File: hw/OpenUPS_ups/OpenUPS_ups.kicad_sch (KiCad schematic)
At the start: 5 parts, among them J101 XT60PW-M, U101 AVR32DB28x-xSO

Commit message: Work on Buck Boosts
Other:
- note added: "Analog Out"

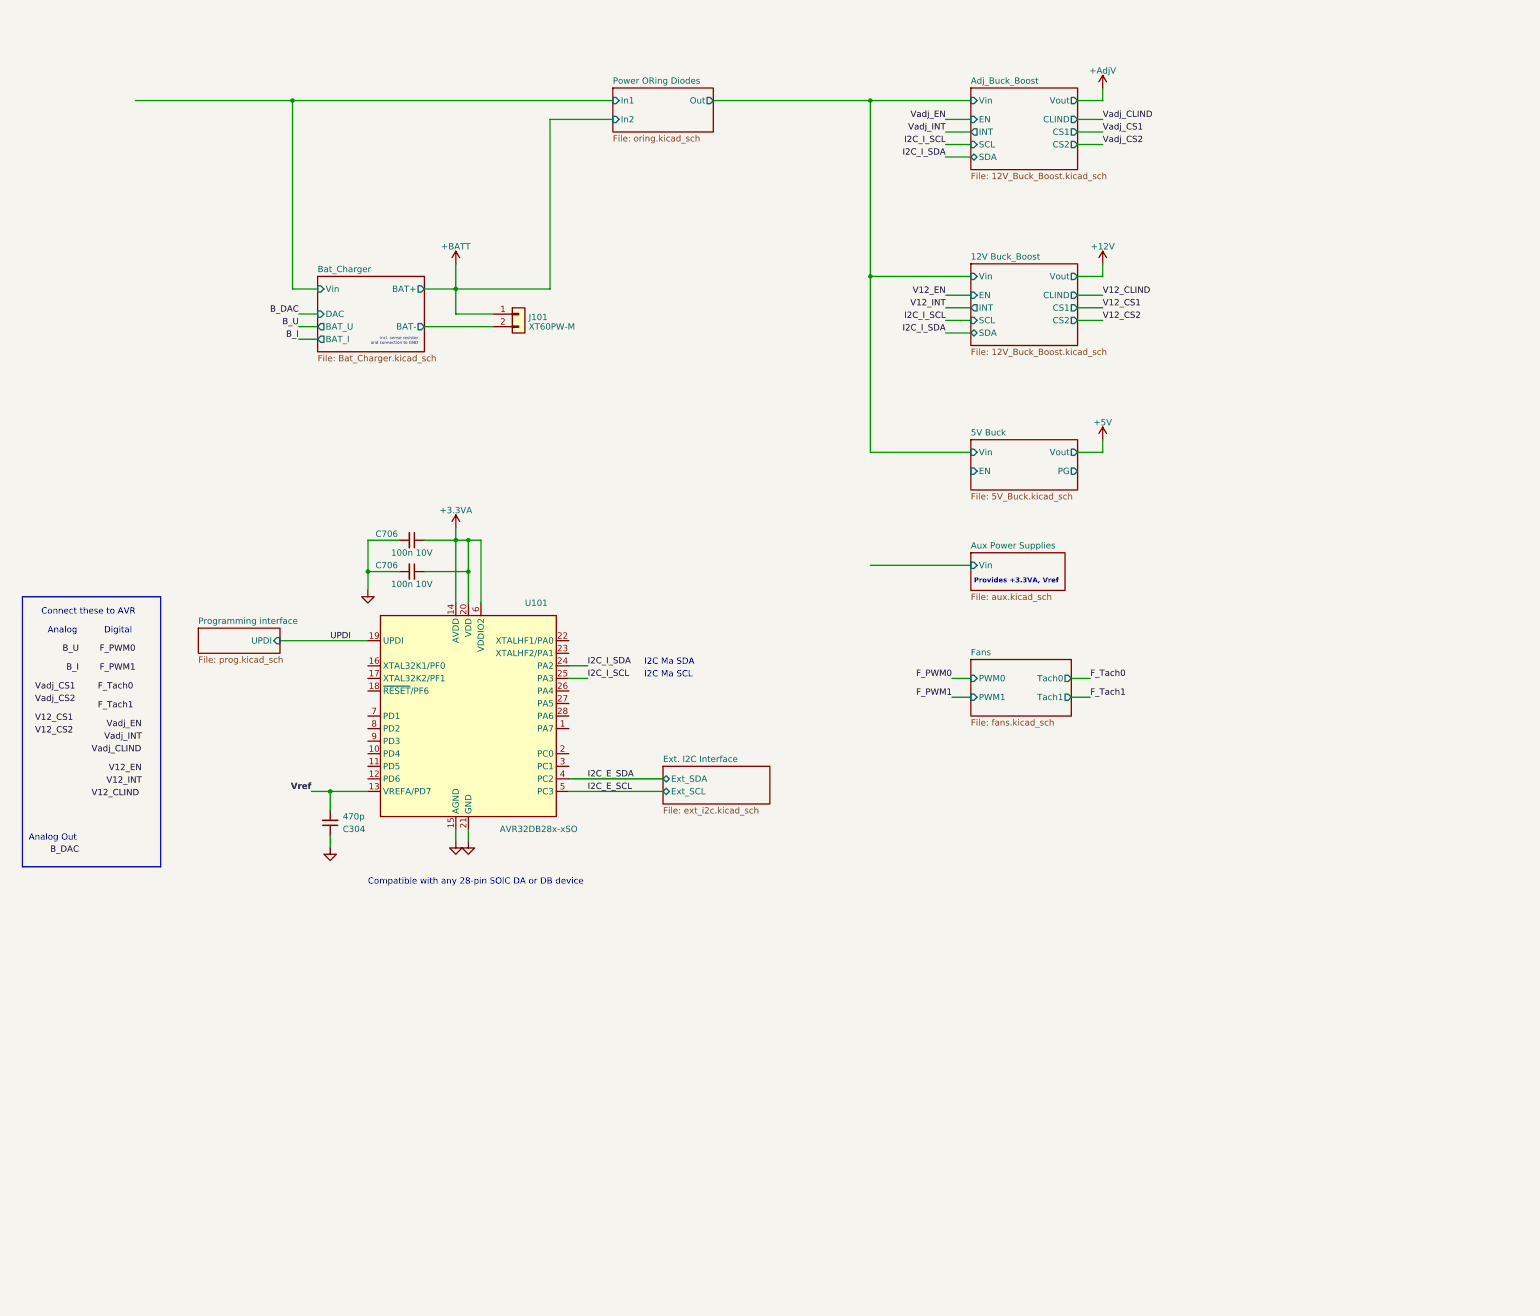
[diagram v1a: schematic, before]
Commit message: Work on 5V; EN pins taken care of.
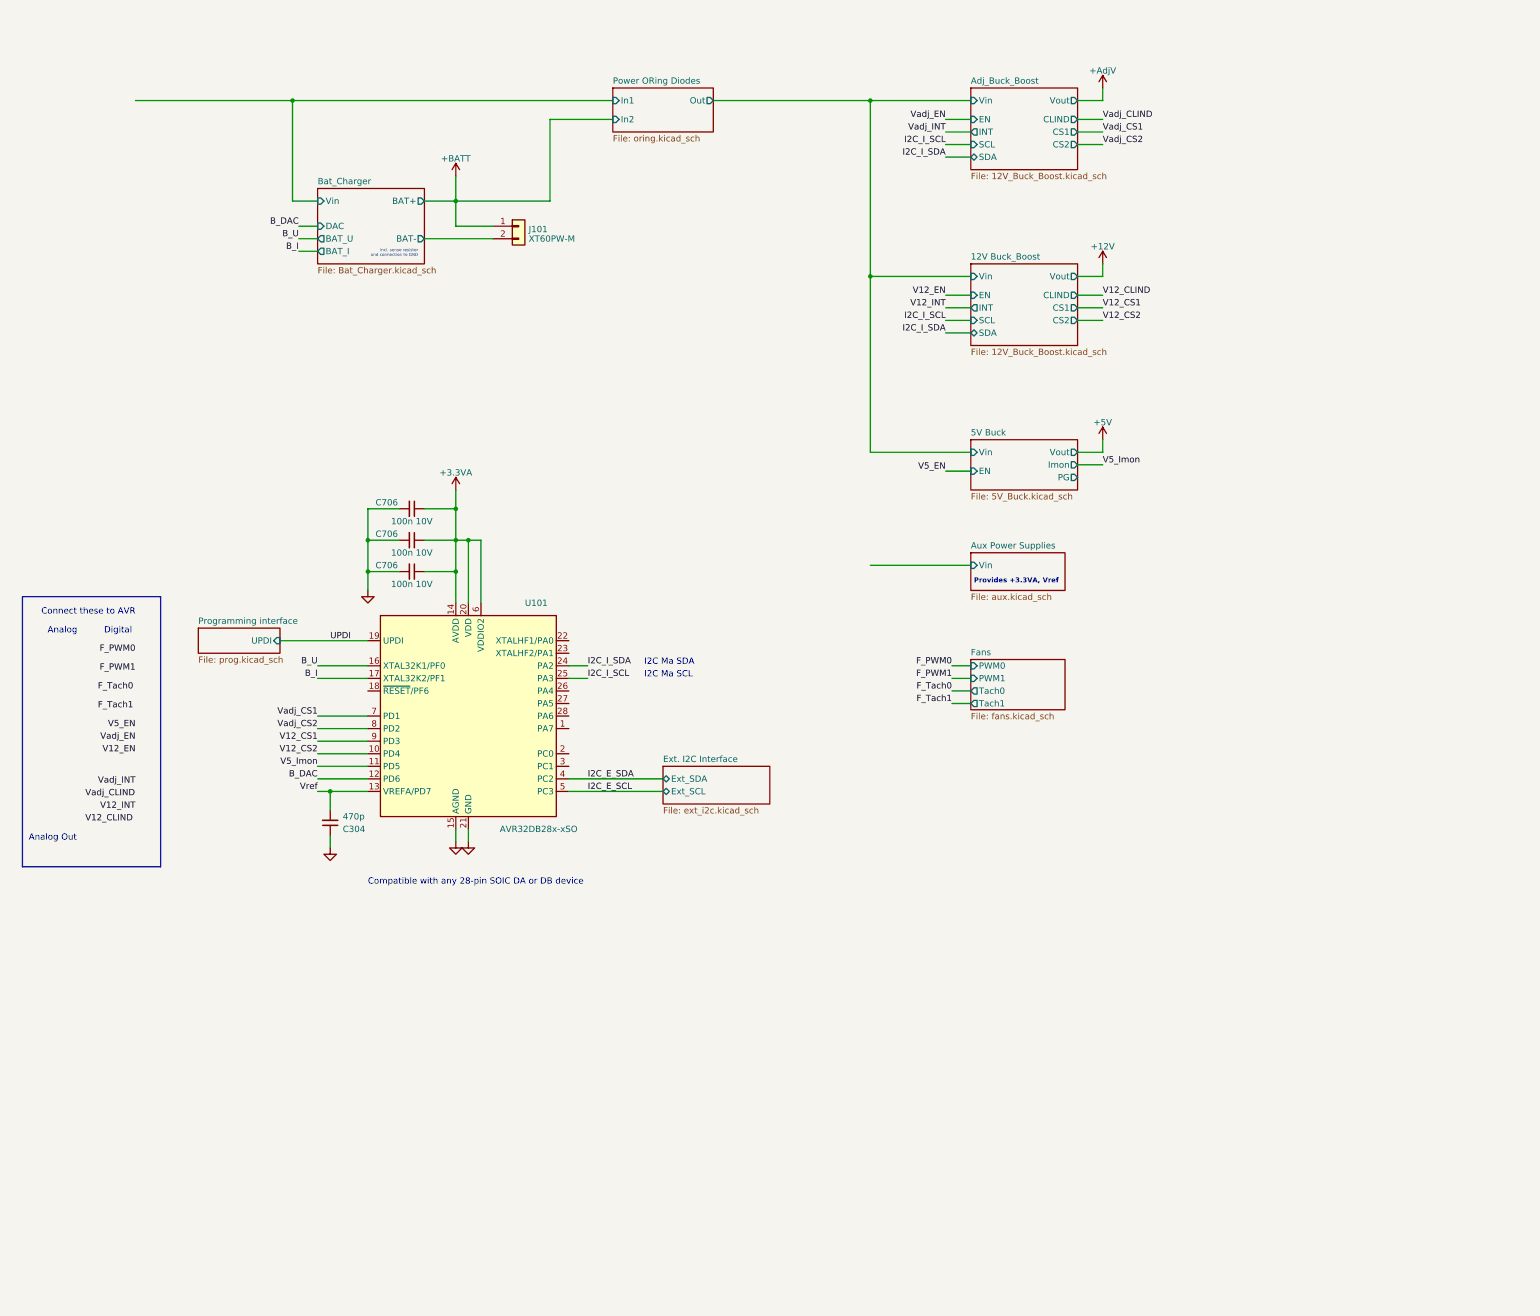
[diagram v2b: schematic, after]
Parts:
- added C706: 100n 10V, Capacitor_SMD:C_0603_1608Metric, symbol Device:C_Small
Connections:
- net +3.3VA: now also C706.1
- net B_DAC: now also U101.12 (PD6)
- net B_I: now also U101.17 (XTAL32K2/PF1)
- net B_U: now also U101.16 (XTAL32K1/PF0)
- net GND: now also C706.2
- net V12_CS1: now also U101.9 (PD3)
- net V12_CS2: now also U101.10 (PD4)
- net Vadj_CS1: now also U101.7 (PD1)
- net Vadj_CS2: now also U101.8 (PD2)
- net V5_Imon: now reaches U101.11 (PD5)
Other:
- sheet 5V Buck ports: added Imon; removed none
- moved on the sheet: J101

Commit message: Added ports and fuses
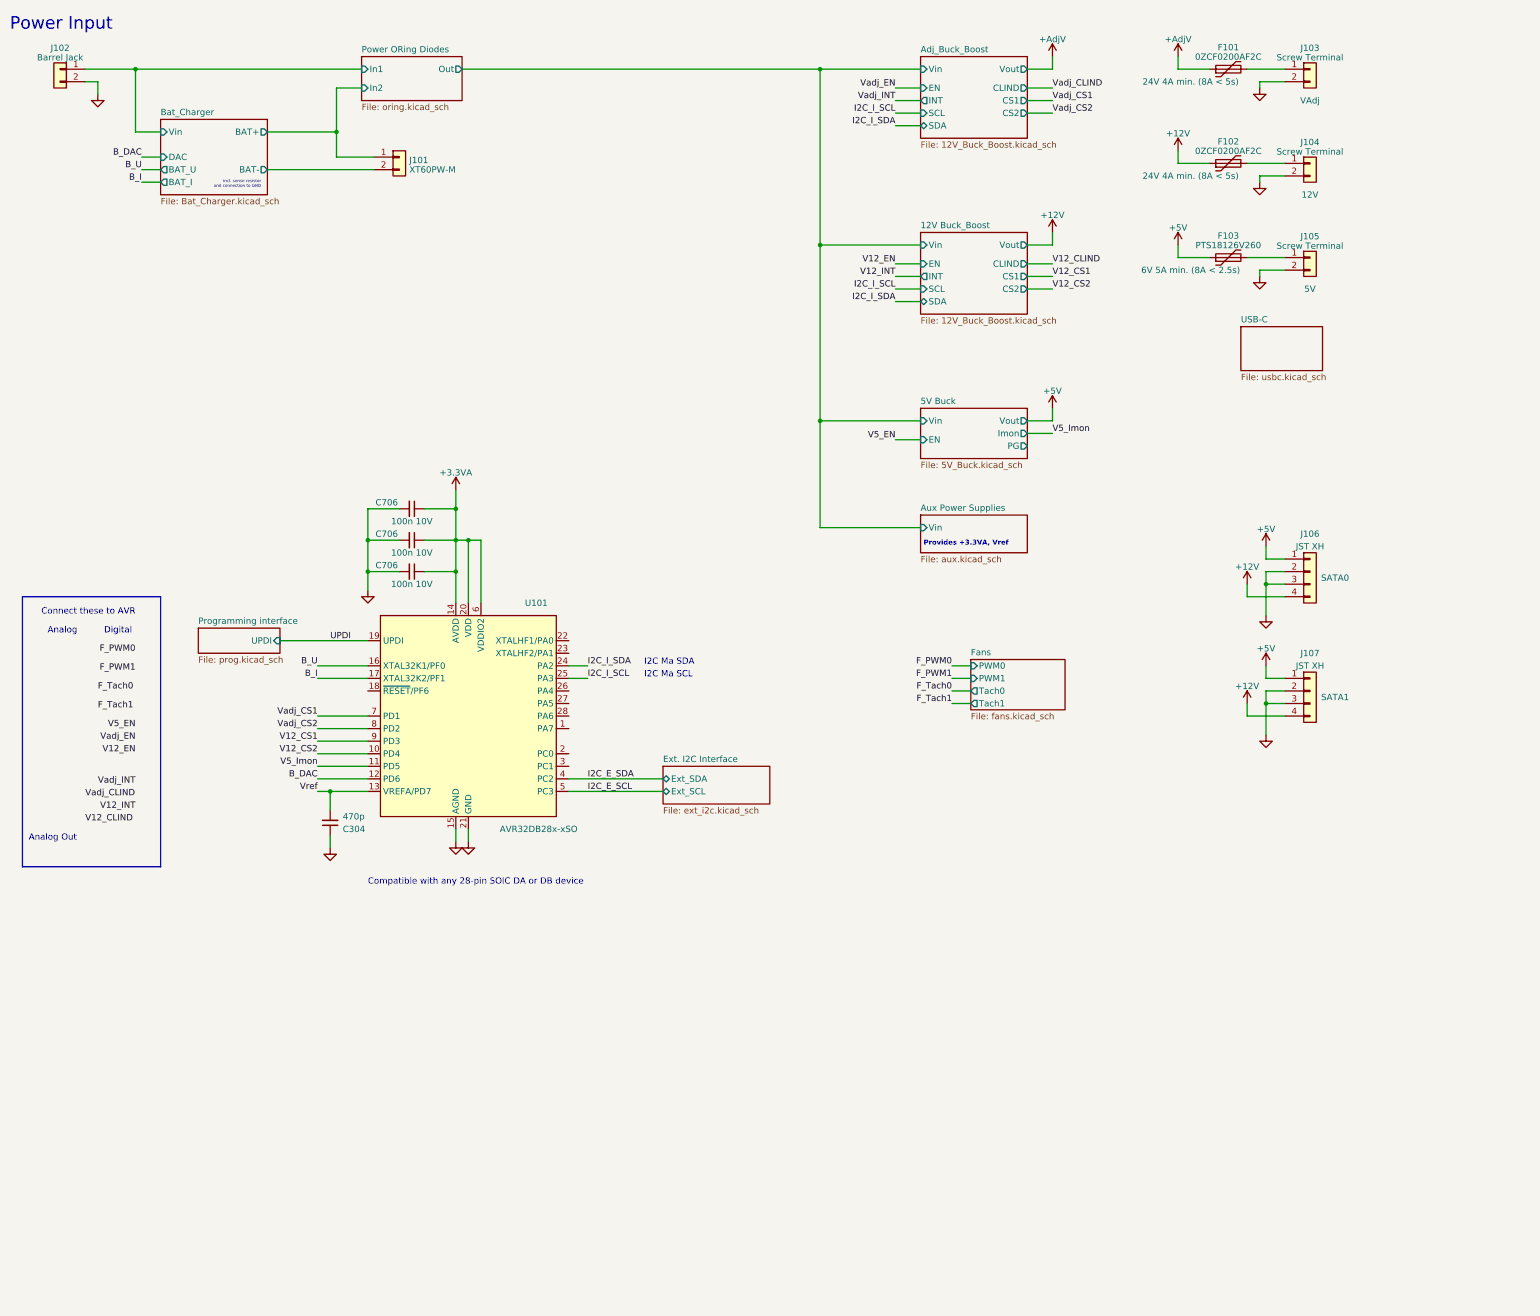
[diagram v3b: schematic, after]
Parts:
- added F101, F102: 0ZCF0200AF2C, Fuse:Fuse_2920_7451Metric, symbol Device:Polyfuse
- added F103: PTS18126V260, Fuse:Fuse_1812_4532Metric, symbol Device:Polyfuse
- added J102: Barrel Jack, Connector_BarrelJack:BarrelJack_CUI_PJ-063AH_Horizontal, symbol Connector_Generic:Conn_01x02
- added J103, J104, J105: Screw Terminal, screw_term:691213710002, symbol Connector_Generic:Conn_01x02
- added J106, J107: JST XH, Connector_JST:JST_XH_S4B-XH-A_1x04_P2.50mm_Horizontal, symbol Connector_Generic:Conn_01x04
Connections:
- net +12V: now also F102.1, J106.4 (Pin_4), J107.4 (Pin_4)
- net +5V: now also F103.1, J106.1 (Pin_1), J107.1 (Pin_1)
- net +AdjV: now also F101.1
- net Bat_Charger/Vin: now also J102.1 (Pin_1)
- net GND: now also J102.2 (Pin_2), J103.2 (Pin_2), J104.2 (Pin_2), J105.2 (Pin_2), J106.2 (Pin_2), J106.3 (Pin_3), J107.2 (Pin_2), J107.3 (Pin_3)
- net +BATT renamed Bat_Charger/BAT+
- new net: F102.2, J104.1 (Pin_1)
- new net: F101.2, J103.1 (Pin_1)
- new net: F103.2, J105.1 (Pin_1)
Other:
- added sheet USB-C (usbc.kicad_sch)
- note added: "Power Input"
- moved on the sheet: J101

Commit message: Issue #17
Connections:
- net Bat_Charger/Vin renamed Aux Power Supplies/EN2
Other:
- sheet Aux Power Supplies ports: added EN1, EN2; removed none
- moved on the sheet: C304, C706, F101, F102, F103, J101, J102, J103, J104, J105, J106, J107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

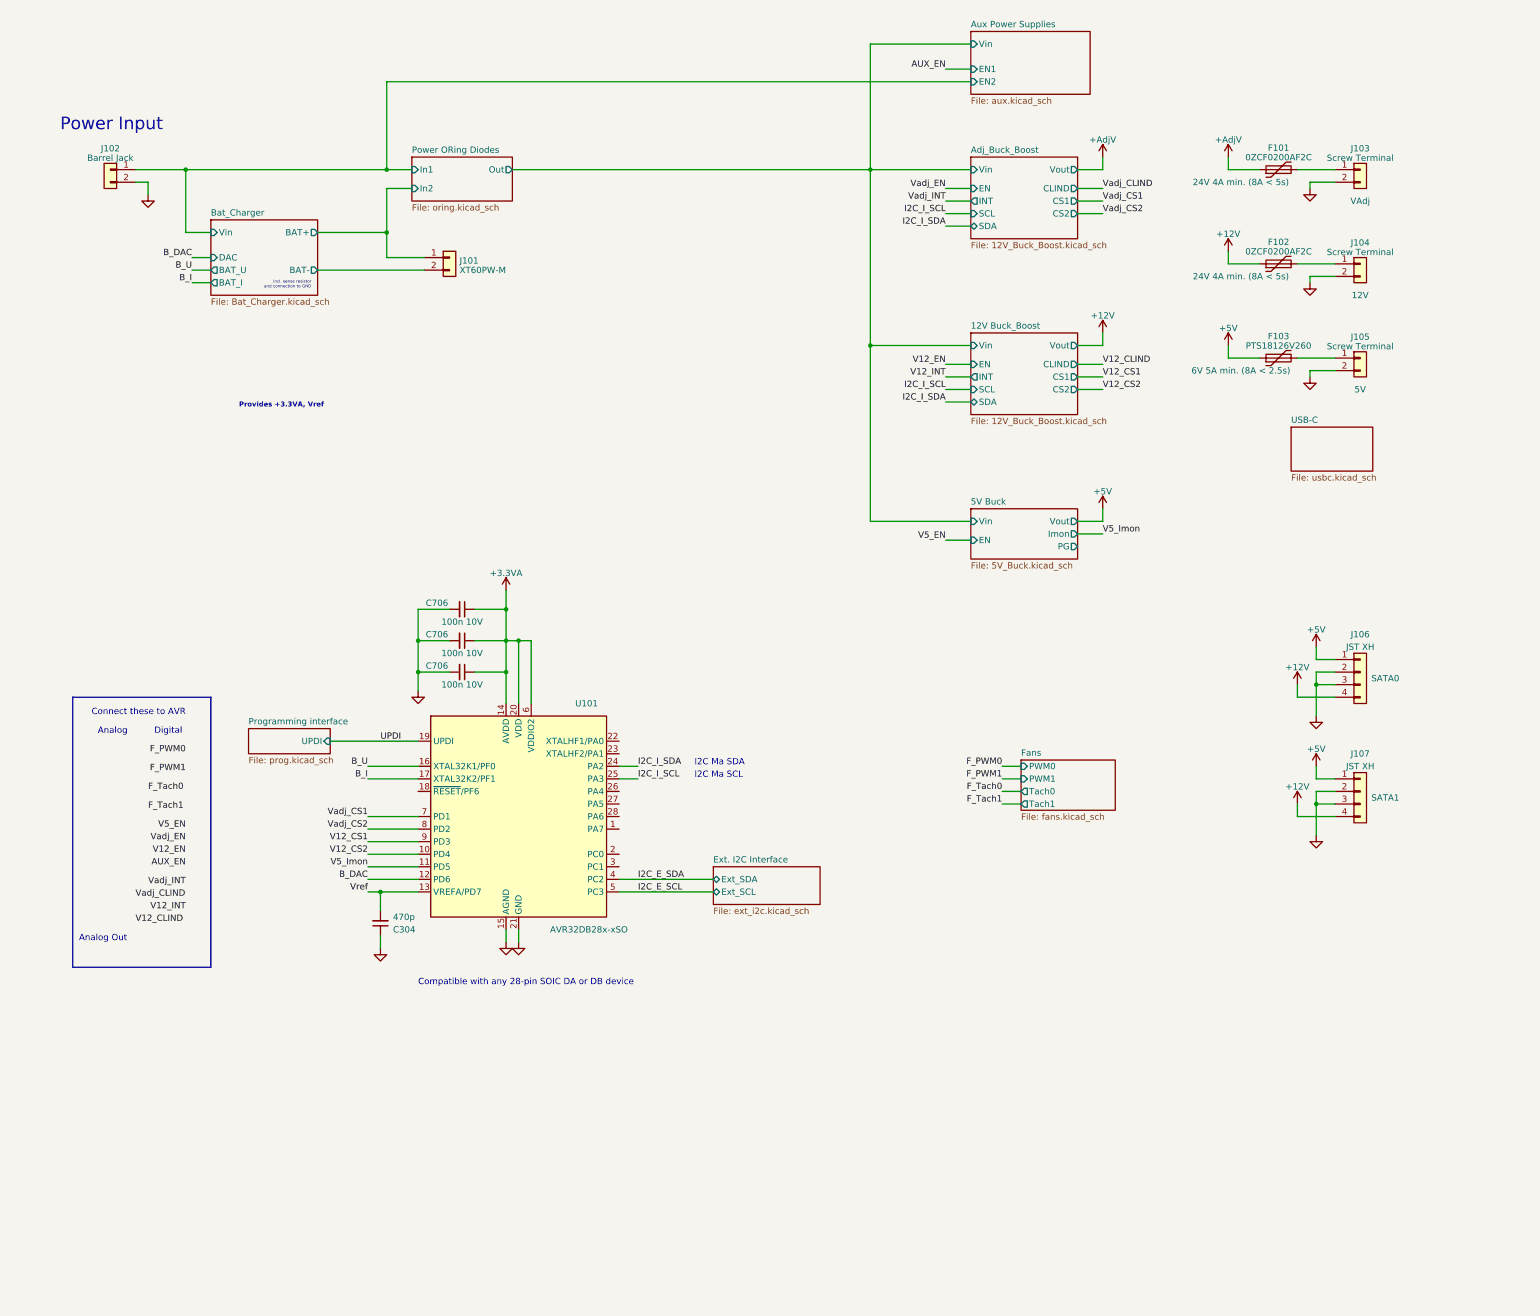
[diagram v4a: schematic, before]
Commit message: Issue #13, USB-C output, at last!
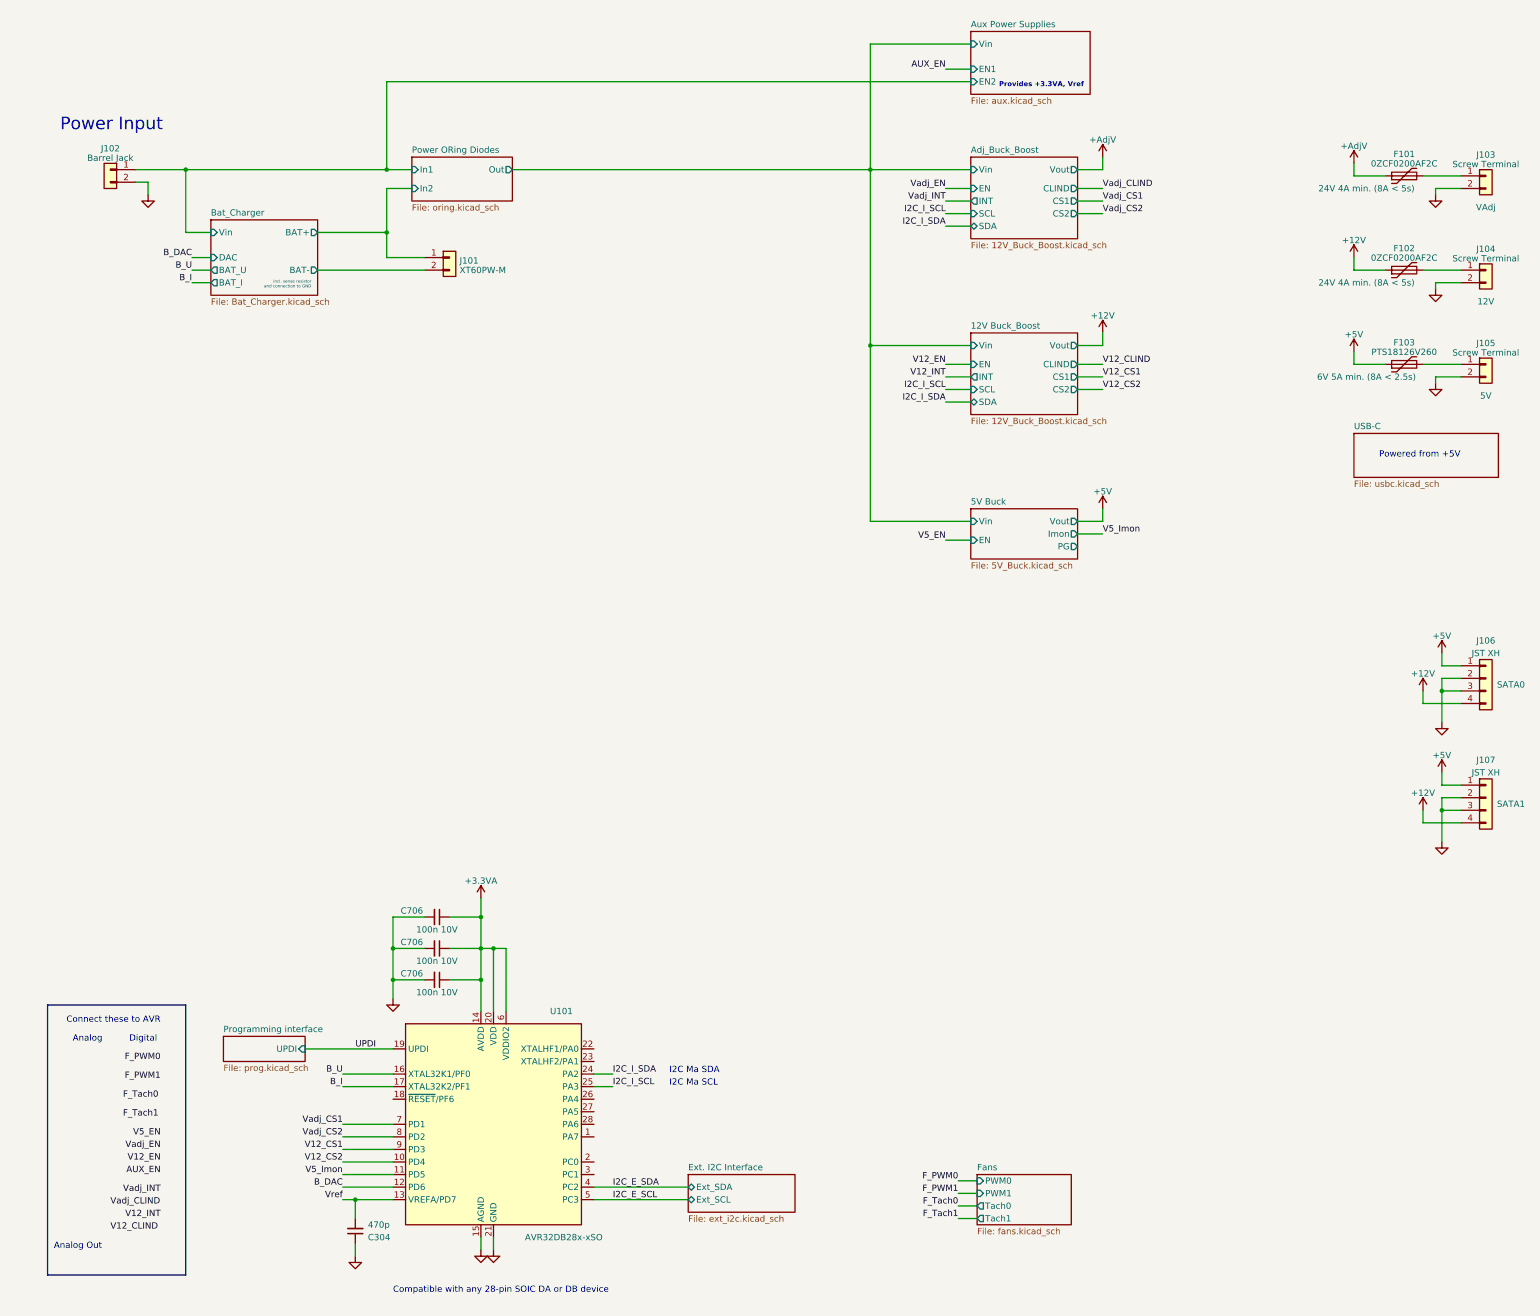
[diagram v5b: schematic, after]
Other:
- note added: "Powered from +5V"
- moved on the sheet: C304, C706, F101, F102, F103, J103, J104, J105, J106, J107, U101
